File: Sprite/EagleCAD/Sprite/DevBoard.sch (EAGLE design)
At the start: 29 parts, among them U1 CC430F5137, U2 HMC5883LSMD, U3 ITG-3200, X1 26 MHz

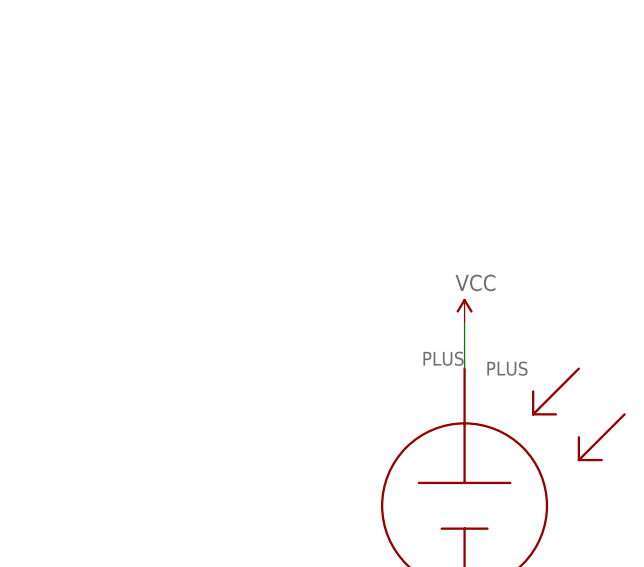
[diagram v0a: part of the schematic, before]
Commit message: Added header to dev board to disconnect solar cells
Added a header to connect/disconnect the solar cells from VCC to allow
programming with the TI launchpad
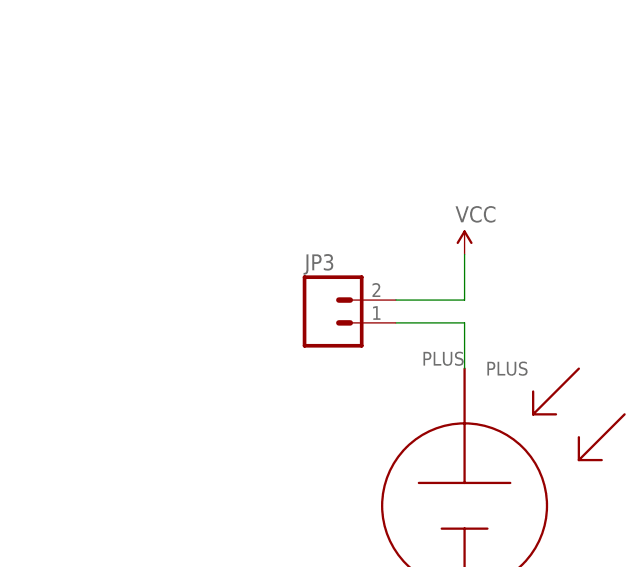
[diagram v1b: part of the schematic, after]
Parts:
- added JP3: (no value), SparkFun:M02PTH
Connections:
- new net VSOLAR: JP3.1, S1.PLUS
- net VCC: now also JP3.2; no longer S1.PLUS
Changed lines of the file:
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@@
 <part name="R5" library="SparkFun" deviceset="RESISTOR" device="0603-RES" value="270R"/>
 <part name="X1" library="ABM11" deviceset="ABM11_CERAMIC_SMD_CRYSTAL" device="ABM11" value="26 MHz"/>
+<part name="JP3" library="SparkFun" deviceset="M02" device="PTH"/>
 </parts>
 <sheets>
@@
 <instances>
 <instance part="GND1" gate="1" x="360.68" y="66.04"/>
-<instance part="P+1" gate="1" x="360.68" y="106.68"/>
+<instance part="P+1" gate="1" x="360.68" y="114.3"/>
 <instance part="U1" gate="G$1" x="152.4" y="86.36"/>
 <instance part="C1" gate="G$1" x="223.52" y="35.56"/>
@@
 <instance part="R5" gate="G$1" x="104.14" y="104.14"/>
 <instance part="X1" gate="X$1" x="236.22" y="43.18"/>
+<instance part="JP3" gate="G$1" x="345.44" y="106.68"/>
 </instances>
 <busses>
@@
 </segment>
 <segment>
-<pinref part="S1" gate="G$1" pin="PLUS"/>
+<pinref part="JP3" gate="G$1" pin="2"/>
 <pinref part="P+1" gate="1" pin="VCC"/>
-<wire x1="360.68" y1="101.6" x2="360.68" y2="106.68" width="0.1524" layer="91"/>
+<wire x1="353.06" y1="109.22" x2="360.68" y2="109.22" width="0.1524" layer="91"/>
+<wire x1="360.68" y1="109.22" x2="360.68" y2="114.3" width="0.1524" layer="91"/>
 </segment>
 </net>
@@
 </segment>
 </net>
+<net name="VSOLAR" class="0">
+<segment>
+<pinref part="JP3" gate="G$1" pin="1"/>
+<pinref part="S1" gate="G$1" pin="PLUS"/>
+<wire x1="353.06" y1="106.68" x2="360.68" y2="106.68" width="0.1524" layer="91"/>
+<wire x1="360.68" y1="106.68" x2="360.68" y2="101.6" width="0.1524" layer="91"/>
+</segment>
+</net>

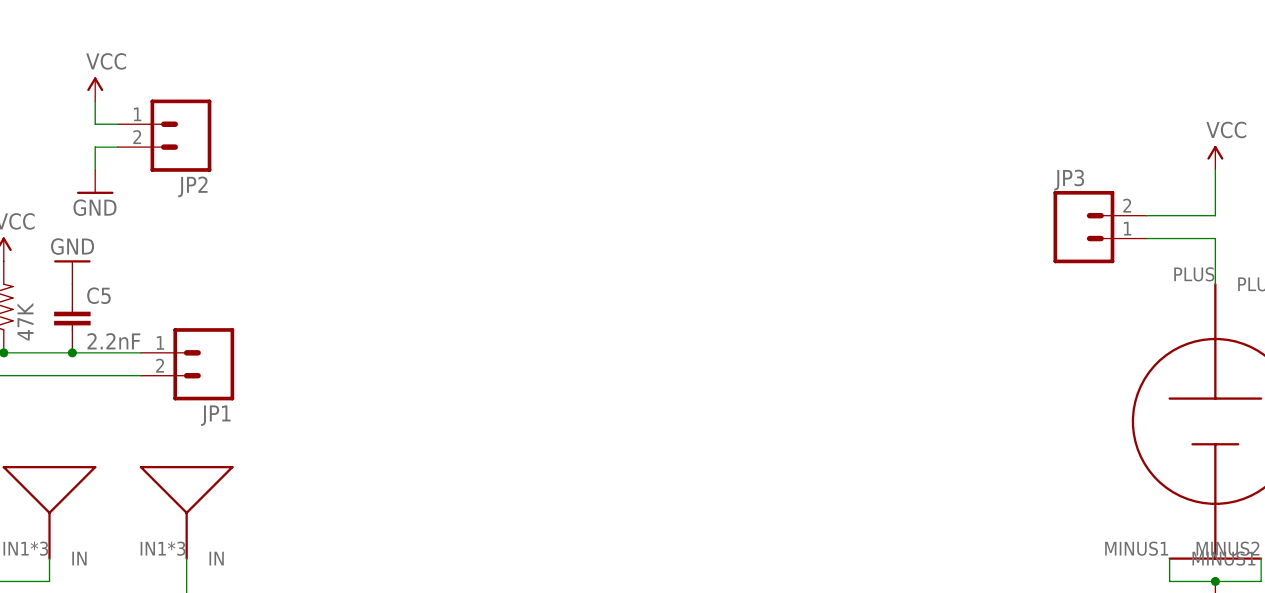
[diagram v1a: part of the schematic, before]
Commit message: Added headers for serial port
Put an extra pair of headers on the board to interface with a serial
port for Energia debugging.  Still have to figure out which MCU pins to
use
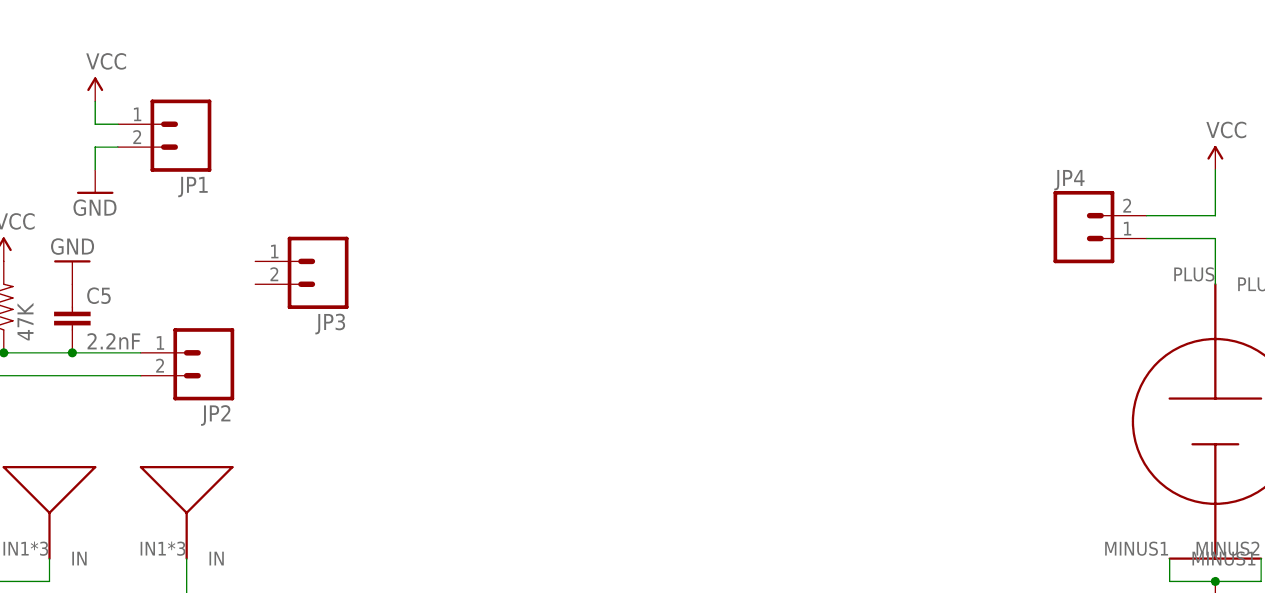
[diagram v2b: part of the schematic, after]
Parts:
- added JP4: (no value), SparkFun:M02PTH
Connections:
- net GND: now also JP1.2; no longer JP2.2
- net RST: now also JP2.1; no longer JP1.1
- net TEST: now also JP2.2; no longer JP1.2
- net VCC: now also JP1.1, JP4.2; no longer JP2.1, JP3.2
- net VSOLAR: now also JP4.1; no longer JP3.1
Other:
- moved on the sheet: JP1, JP2, JP3
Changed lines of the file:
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@@
 <part name="GND20" library="SparkFun" deviceset="GND" device=""/>
 <part name="GND21" library="SparkFun" deviceset="GND" device=""/>
+<part name="JP2" library="SparkFun" deviceset="M02" device="PTH"/>
 <part name="JP1" library="SparkFun" deviceset="M02" device="PTH"/>
-<part name="JP2" library="SparkFun" deviceset="M02" device="PTH"/>
 <part name="GND16" library="SparkFun" deviceset="GND" device=""/>
 <part name="P+4" library="SparkFun" deviceset="VCC" device=""/>
@@
 <part name="R5" library="SparkFun" deviceset="RESISTOR" device="0603-RES" value="270R"/>
 <part name="X1" library="ABM11" deviceset="ABM11_CERAMIC_SMD_CRYSTAL" device="ABM11" value="26 MHz"/>
+<part name="JP4" library="SparkFun" deviceset="M02" device="PTH"/>
 <part name="JP3" library="SparkFun" deviceset="M02" device="PTH"/>
 </parts>
@@
 <instance part="GND20" gate="1" x="322.58" y="180.34"/>
 <instance part="GND21" gate="1" x="203.2" y="88.9" rot="R180"/>
-<instance part="JP1" gate="G$1" x="248.92" y="93.98" rot="R180"/>
-<instance part="JP2" gate="G$1" x="246.38" y="119.38" rot="R180"/>
+<instance part="JP2" gate="G$1" x="248.92" y="93.98" rot="R180"/>
+<instance part="JP1" gate="G$1" x="246.38" y="119.38" rot="R180"/>
 <instance part="GND16" gate="1" x="236.22" y="111.76"/>
 <instance part="P+4" gate="1" x="236.22" y="121.92"/>
@@
 <instance part="R5" gate="G$1" x="104.14" y="104.14"/>
 <instance part="X1" gate="X$1" x="236.22" y="43.18"/>
-<instance part="JP3" gate="G$1" x="345.44" y="106.68"/>
+<instance part="JP4" gate="G$1" x="345.44" y="106.68"/>
+<instance part="JP3" gate="G$1" x="261.62" y="104.14" rot="R180"/>
 </instances>
 <busses>
@@
 </segment>
 <segment>
-<pinref part="JP2" gate="G$1" pin="1"/>
+<pinref part="JP1" gate="G$1" pin="1"/>
 <pinref part="P+4" gate="1" pin="VCC"/>
 <wire x1="238.76" y1="119.38" x2="236.22" y2="119.38" width="0.1524" layer="91"/>
@@
 </segment>
 <segment>
-<pinref part="JP3" gate="G$1" pin="2"/>
+<pinref part="JP4" gate="G$1" pin="2"/>
 <pinref part="P+1" gate="1" pin="VCC"/>
 <wire x1="353.06" y1="109.22" x2="360.68" y2="109.22" width="0.1524" layer="91"/>
@@
 </segment>
 <segment>
-<pinref part="JP2" gate="G$1" pin="2"/>
+<pinref part="JP1" gate="G$1" pin="2"/>
 <pinref part="GND16" gate="1" pin="GND"/>
 <wire x1="238.76" y1="116.84" x2="236.22" y2="116.84" width="0.1524" layer="91"/>
@@
 <wire x1="175.26" y1="93.98" x2="226.06" y2="93.98" width="0.1524" layer="91"/>
 <pinref part="U1" gate="G$1" pin="40"/>
-<pinref part="JP1" gate="G$1" pin="1"/>
+<pinref part="JP2" gate="G$1" pin="1"/>
 <pinref part="R2" gate="G$1" pin="1"/>
 <wire x1="226.06" y1="93.98" x2="233.68" y2="93.98" width="0.1524" layer="91"/>
@@
 <wire x1="175.26" y1="91.44" x2="241.3" y2="91.44" width="0.1524" layer="91"/>
 <pinref part="U1" gate="G$1" pin="39"/>
-<pinref part="JP1" gate="G$1" pin="2"/>
+<pinref part="JP2" gate="G$1" pin="2"/>
 </segment>
 </net>
@@
 <net name="VSOLAR" class="0">
 <segment>
-<pinref part="JP3" gate="G$1" pin="1"/>
+<pinref part="JP4" gate="G$1" pin="1"/>
 <pinref part="S1" gate="G$1" pin="PLUS"/>
 <wire x1="353.06" y1="106.68" x2="360.68" y2="106.68" width="0.1524" layer="91"/>

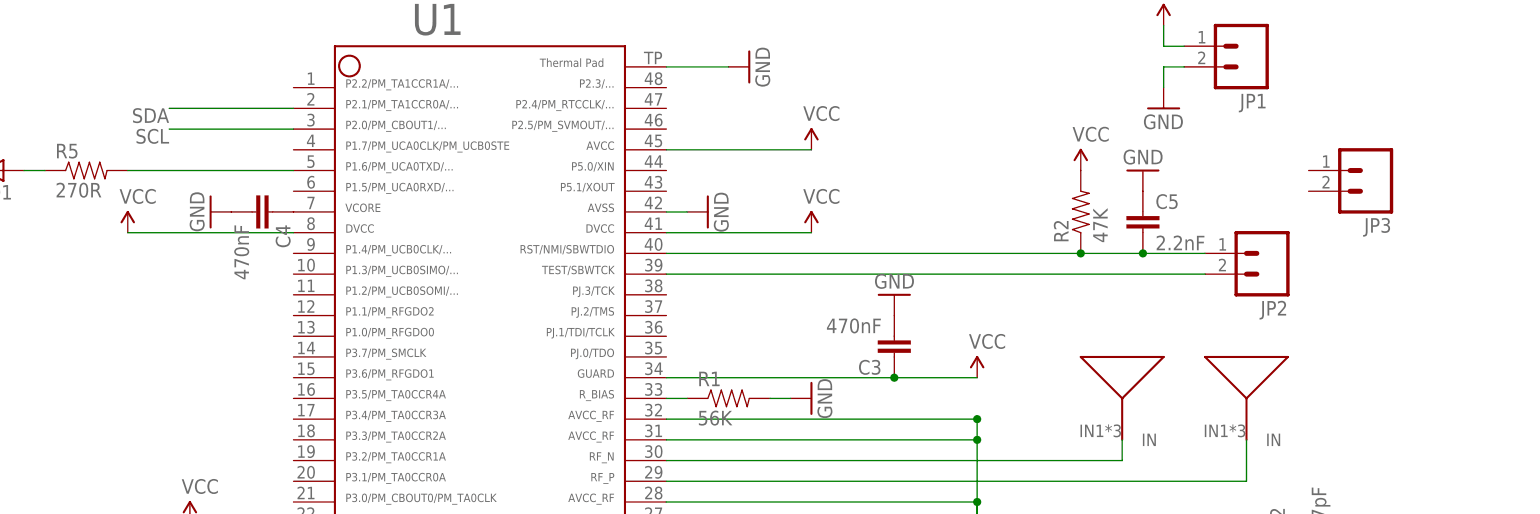
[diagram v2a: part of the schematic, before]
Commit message: Connected serial pins on dev board
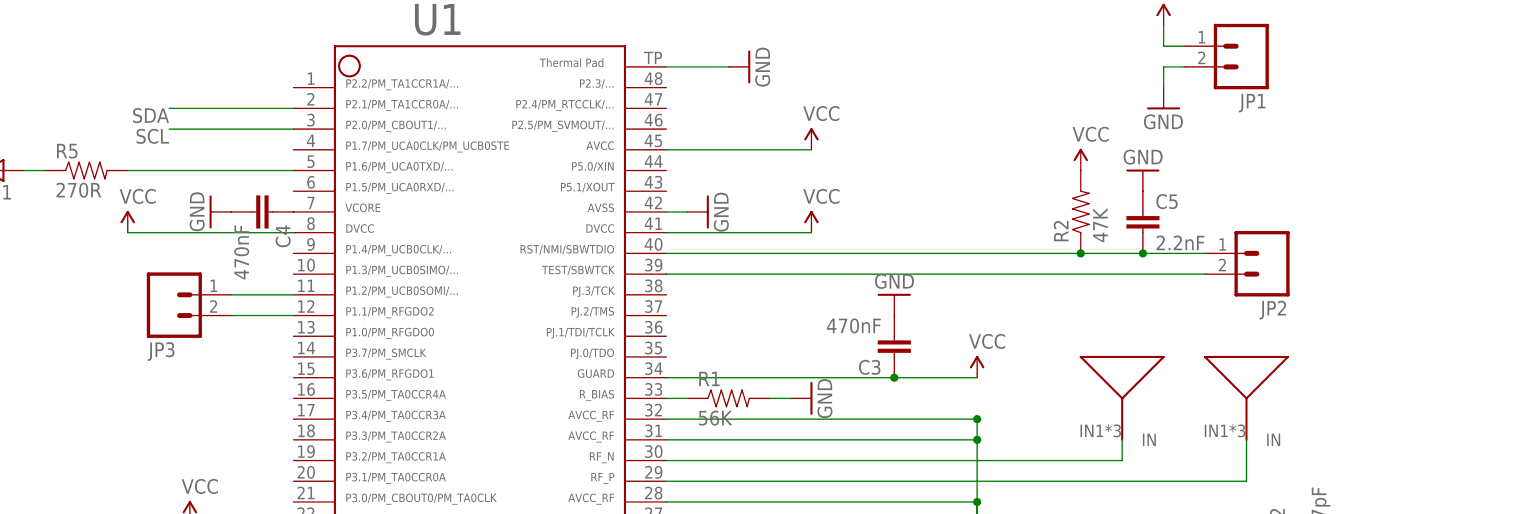
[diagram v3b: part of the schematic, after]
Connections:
- new net N$12: JP3.1, U1.11
- new net N$13: JP3.2, U1.12
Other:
- moved on the sheet: JP3
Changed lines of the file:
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@@
 <instance part="X1" gate="X$1" x="236.22" y="43.18"/>
 <instance part="JP4" gate="G$1" x="345.44" y="106.68"/>
-<instance part="JP3" gate="G$1" x="261.62" y="104.14" rot="R180"/>
+<instance part="JP3" gate="G$1" x="114.3" y="88.9" rot="MR180"/>
 </instances>
 <busses>
@@
 </segment>
 </net>
+<net name="N$12" class="0">
+<segment>
+<pinref part="JP3" gate="G$1" pin="1"/>
+<pinref part="U1" gate="G$1" pin="11"/>
+<wire x1="121.92" y1="88.9" x2="129.54" y2="88.9" width="0.1524" layer="91"/>
+</segment>
+</net>
+<net name="N$13" class="0">
+<segment>
+<pinref part="JP3" gate="G$1" pin="2"/>
+<pinref part="U1" gate="G$1" pin="12"/>
+<wire x1="121.92" y1="86.36" x2="129.54" y2="86.36" width="0.1524" layer="91"/>
+</segment>
+</net>

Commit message: Programmer Board
Finished programmer shield board
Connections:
- net N$12 renamed RX
- net N$13 renamed TX
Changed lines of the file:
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@@
 </segment>
 </net>
-<net name="N$12" class="0">
+<net name="RX" class="0">
 <segment>
 <pinref part="JP3" gate="G$1" pin="1"/>
@@
 </segment>
 </net>
-<net name="N$13" class="0">
+<net name="TX" class="0">
 <segment>
 <pinref part="JP3" gate="G$1" pin="2"/>

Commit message: Finished Programmer Board
Added KickSat Silkscreen
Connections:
- net RX renamed TXD
- net TX renamed RXD
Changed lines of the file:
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@@
 </segment>
 </net>
-<net name="RX" class="0">
+<net name="TXD" class="0">
 <segment>
 <pinref part="JP3" gate="G$1" pin="1"/>
@@
 </segment>
 </net>
-<net name="TX" class="0">
+<net name="RXD" class="0">
 <segment>
 <pinref part="JP3" gate="G$1" pin="2"/>
